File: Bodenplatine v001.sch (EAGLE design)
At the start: 3 parts, among them K8 RY210005

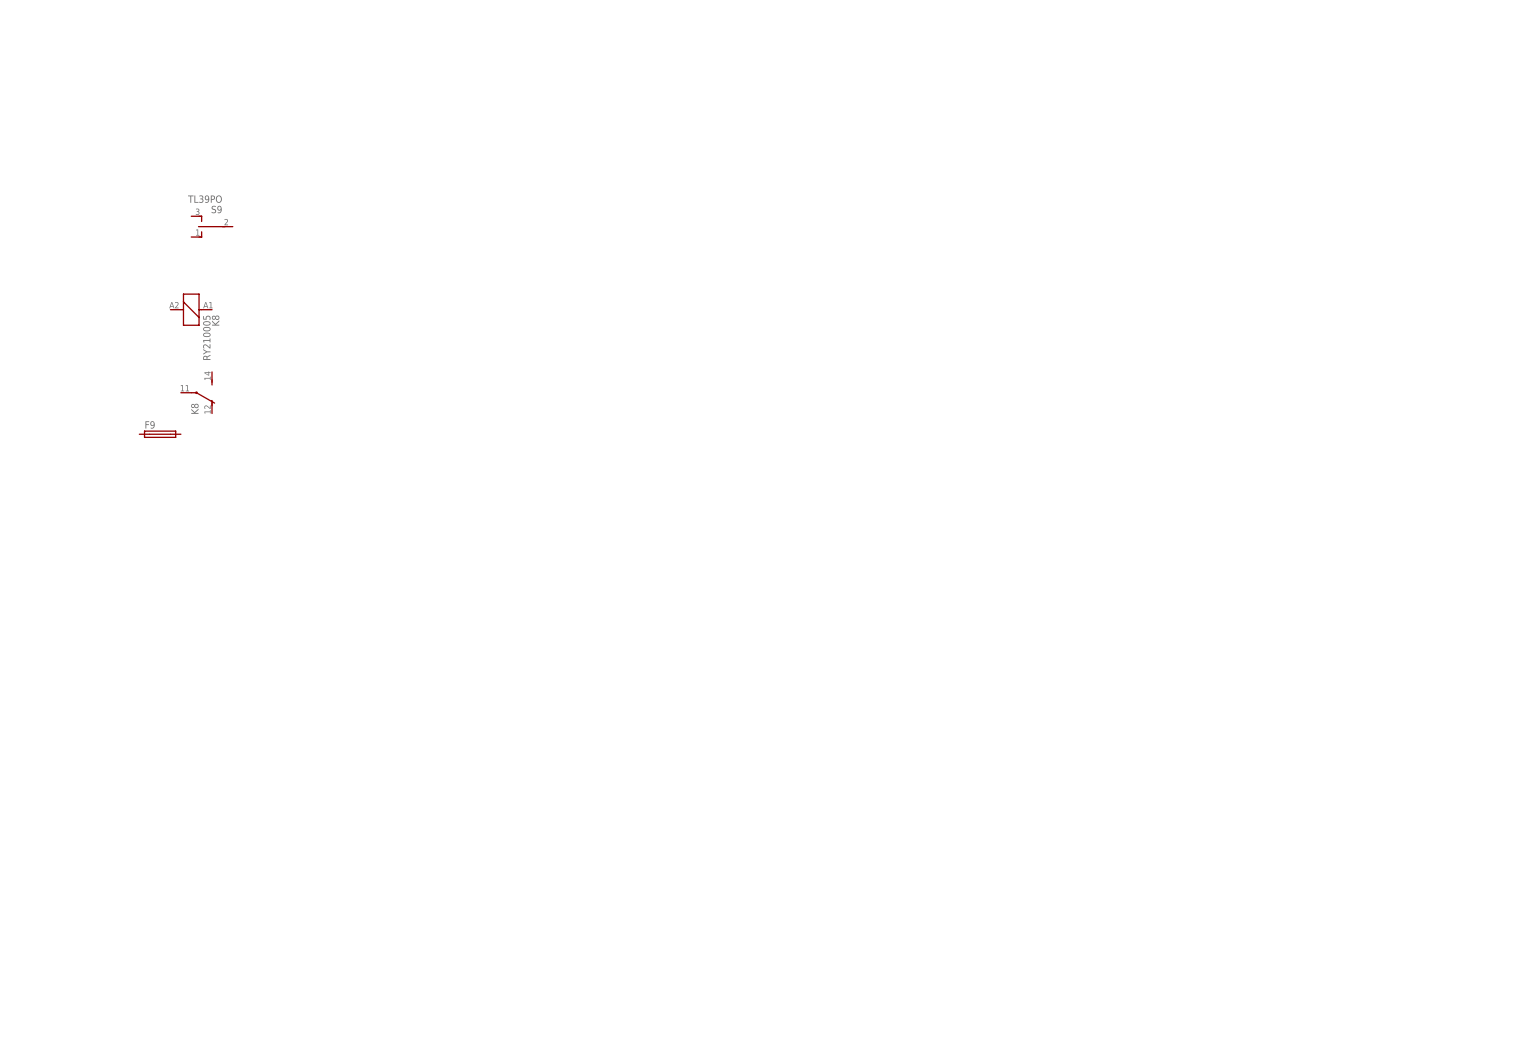
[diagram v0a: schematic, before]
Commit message: Erste fast fertige Version des Schaltplans der Bodebplatine
Es fehlt nur noch die Wago Klemme für L/N/PE Netzteil und 12V+/-
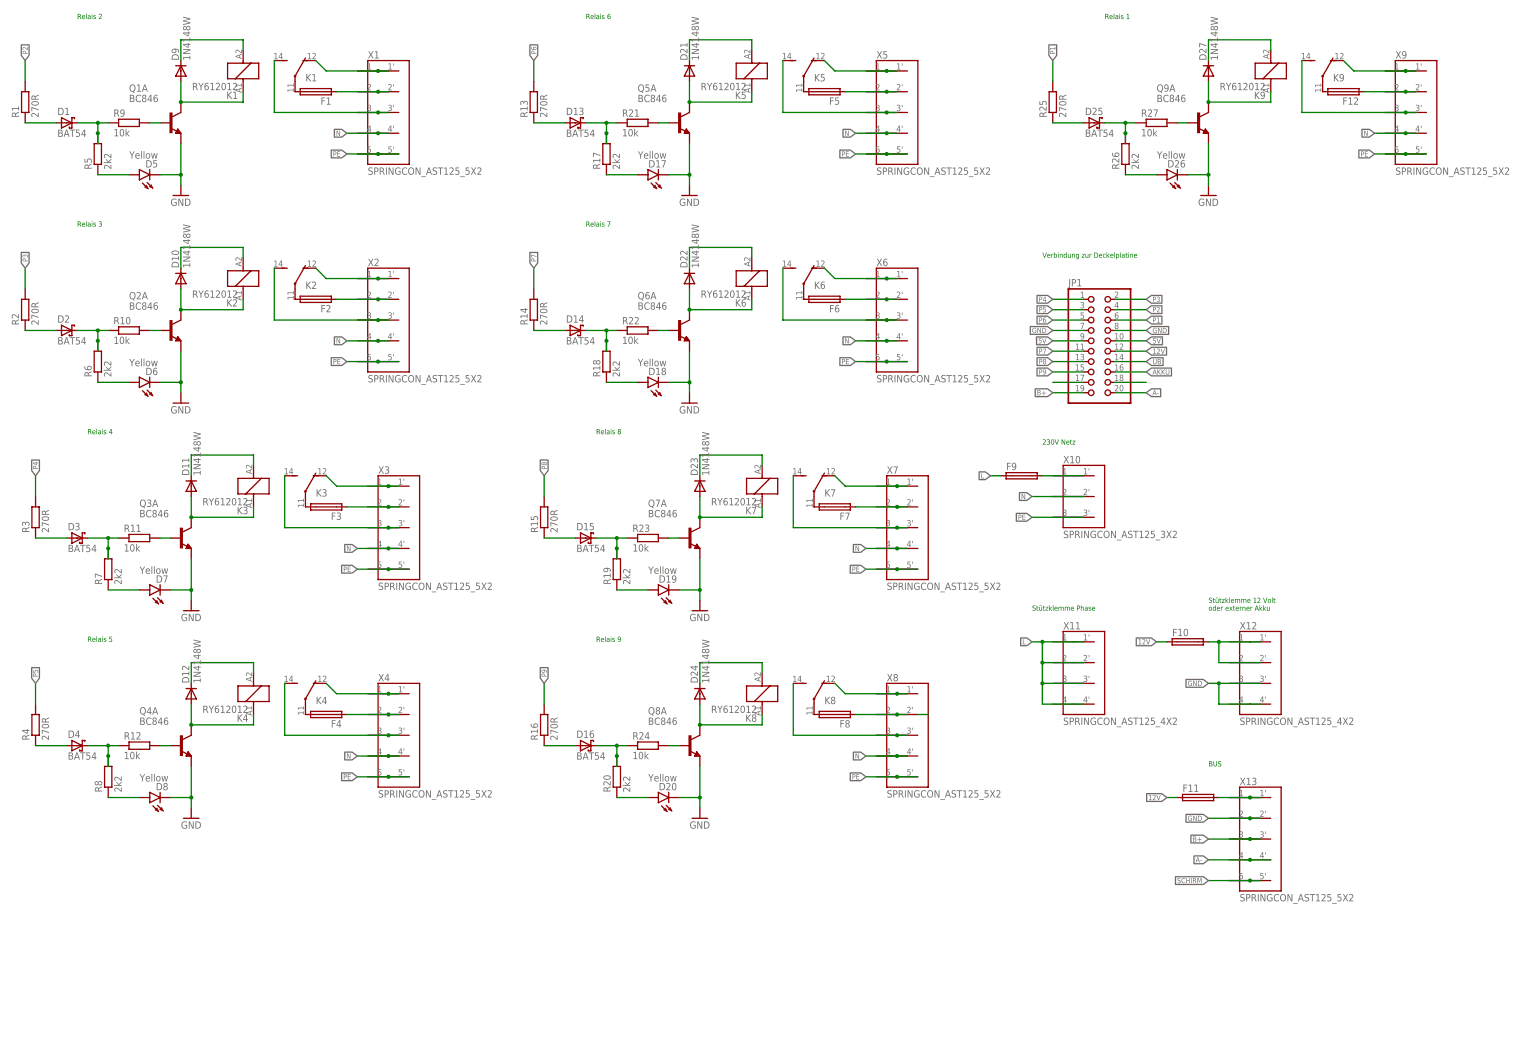
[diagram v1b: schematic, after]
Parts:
- removed S9: TL39PO, xMZ-Mod-Touch-Bodenplatine:TL39PO
- added D1, D13, D14, D15, D16, D2, D25, D3, D4: BAT54, diode:BAT54
- added D10, D11, D12, D21, D22, D23, D24, D27, D9: 1N4148W, diode:1N4148DO35-7
- added D17, D18, D19, D20, D26, D5, D6, D7, D8: Yellow, SparkFun-LED:LED-YELLOW0603
- added F1, F10, F11, F12, F2, F3, F4, F5, F6, F7, F8: (no value), xMZ-Mod-Touch-Bodenplatine:F456
- added JP1: (no value), pinhead:PINHD-2X10
- added K1, K2, K3, K4, K5, K6, K7, K9: RY612012, xMZ-Mod-Touch-Bodenplatine:RY612012
- added Q1, Q2, Q3, Q4, Q5, Q6, Q7, Q8, Q9: BC846, AWJLEagleLib:BC846BS"
- added R1, R13, R14, R15, R16, R2, R25, R3, R4: 270R, rcl:R-EU_M0805
- added R10, R11, R12, R21, R22, R23, R24, R27, R9: 10k, rcl:R-EU_R0603
- added R17, R18, R19, R20, R26, R5, R6, R7, R8: 2k2, rcl:R-EU_R0603
- added X1, X13, X2, X3, X4, X5, X6, X7, X8, X9: SPRINGCON_AST125_5X2, xMZ-Mod-Touch-Bodenplatine:SPRINGCON_AST125_5X2
- added X10: SPRINGCON_AST125_3X2, xMZ-Mod-Touch-Bodenplatine:SPRINGCON_AST125_3X2
- added X11, X12: SPRINGCON_AST125_4X2, xMZ-Mod-Touch-Bodenplatine:SPRINGCON_AST125_4X2
- K8: value RY210005 -> RY612012; device xMZ-Mod-Touch-Bodenplatine:RY210005 -> xMZ-Mod-Touch-Bodenplatine:RY612012
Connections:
- new net 12V: F10.1, F11.1, JP1.12
- new net 5V: JP1.10, JP1.9
- new net A-: JP1.20, X13.4@1, X13.4@2
- new net AKKU: JP1.16
- new net B+: JP1.19, X13.3@1
- new net GND: D17.C, D18.C, D19.C, D20.C, D26.C, D5.C, D6.C, D7.C, D8.C, JP1.7, JP1.8, Q1A.E, Q2A.E, Q3A.E, Q4A.E, Q5A.E, Q6A.E, Q7A.E, Q8A.E, Q9A.E, X13.2@1
- new net L: F9.1
- new net N: X1.4@1, X2.4@1, X3.4@1, X4.4@1, X5.4@1, X6.4@1, X7.4@1, X8.4@1, X9.4@1
- new net N$1: F1.1, X1.2@1
- new net N$10: Q1A.B, R9.2
- new net N$108: JP1.17
- new net N$11: D9.C, K11.2
- new net N$12: F2.2, K22.P
- new net N$13: D2.A, R2.1
- new net N$14: D2.C, R10.1, R6.2
- new net N$15: D6.A, R6.1
- new net N$16: Q2A.B, R10.2
- new net N$17: D10.C, K21.2
- new net N$18: D10.A, K21.1, Q2A.C
- new net N$19: F2.1, X2.2@1
- new net N$2: K12.S, X1.3@1
- new net N$20: K22.O, X2.1@1
- new net N$21: K32.S, X3.3@1
- new net N$22: F3.2, K32.P
- new net N$23: D3.A, R3.1
- new net N$24: D3.C, R11.1, R7.2
- new net N$25: D7.A, R7.1
- new net N$26: Q3A.B, R11.2
- new net N$27: D11.C, K31.2
- new net N$28: D11.A, K31.1, Q3A.C
- new net N$29: F3.1, X3.2@1
- new net N$3: F1.2, K12.P
- new net N$30: K32.O, X3.1@1
- new net N$31: K42.S, X4.3@1
- new net N$32: F4.2, K42.P
- new net N$33: D4.A, R4.1
- new net N$34: D4.C, R12.1, R8.2
- new net N$35: D8.A, R8.1
- new net N$36: Q4A.B, R12.2
- new net N$37: D12.C, K41.2
- new net N$38: D12.A, K41.1, Q4A.C
- new net N$39: F4.1, X4.2@1
- new net N$4: K12.O, X1.1@1
- new net N$40: K42.O, X4.1@1
- new net N$41: K52.S, X5.3@1
- new net N$42: F5.2, K52.P
- new net N$43: D13.A, R13.1
- new net N$44: D13.C, R17.2, R21.1
- new net N$45: D17.A, R17.1
- new net N$46: Q5A.B, R21.2
- new net N$47: D21.C, K51.2
- new net N$48: D21.A, K51.1, Q5A.C
- new net N$49: F5.1, X5.2@1
- new net N$5: D9.A, K11.1, Q1A.C
- new net N$50: K52.O, X5.1@1
- new net N$51: K62.S, X6.3@1
- new net N$52: F6.2, K62.P
- new net N$53: D14.A, R14.1
- new net N$54: D14.C, R18.2, R22.1
- new net N$55: D18.A, R18.1
- new net N$56: Q6A.B, R22.2
- new net N$57: D22.C, K61.2
- new net N$58: D22.A, K61.1, Q6A.C
- new net N$59: F6.1, X6.2@1
- new net N$6: K22.S, X2.3@1
- new net N$60: K62.O, X6.1@1
- new net N$61: K72.S, X7.3@1
- new net N$62: F7.2, K72.P
- new net N$63: D15.A, R15.1
- new net N$64: D15.C, R19.2, R23.1
- new net N$65: D19.A, R19.1
- new net N$66: Q7A.B, R23.2
- new net N$67: D23.C, K71.2
- new net N$68: D23.A, K71.1, Q7A.C
- new net N$69: F7.1, X7.2@1
- new net N$7: D1.A, R1.1
- new net N$70: K72.O, X7.1@1
- new net N$71: K82.S, X8.3@1
- new net N$72: F8.2, K82.P
- new net N$73: D16.A, R16.1
- new net N$74: D16.C, R20.2, R24.1
- new net N$75: D20.A, R20.1
- new net N$76: Q8A.B, R24.2
- new net N$77: D24.C, K81.2
- new net N$78: D24.A, K81.1, Q8A.C
- new net N$79: F8.1, X8.2@1
- new net N$8: D1.C, R5.2, R9.1
- new net N$80: K82.O, X8.1@1
- new net N$81: K92.S, X9.3@1
- new net N$82: F12.2, K92.P
- new net N$83: D25.A, R25.1
- new net N$84: D25.C, R26.2, R27.1
- new net N$85: D26.A, R26.1
- new net N$86: Q9A.B, R27.2
- new net N$87: D27.C, K91.2
- new net N$88: D27.A, K91.1, Q9A.C
- new net N$89: F12.1, X9.2@1
- new net N$9: D5.A, R5.1
- new net N$90: K92.O, X9.1@1
- new net N$91: F9.2
- new net N$92: F11.2, X13.1@1
- new net N$94: F10.2
- new net N$98: JP1.18
- new net P1: JP1.6, R25.2
- new net P2: JP1.4, R1.2
- new net P3: JP1.2, R2.2
- new net P4: JP1.1, R3.2
- new net P5: JP1.3, R4.2
- new net P6: JP1.5, R13.2
- new net P7: JP1.11, R14.2
- new net P8: JP1.13, R15.2
- new net P9: JP1.15, R16.2
- new net PE: X1.5@1, X1.5@2, X2.5@1, X2.5@2, X3.5@1, X3.5@2, X4.5@1, X4.5@2, X5.5@1, X5.5@2, X6.5@1, X6.5@2, X7.5@1, X7.5@2, X8.5@1, X8.5@2, X9.5@1, X9.5@2
- new net SCHIRM: X13.5@1
- new net UB: JP1.14
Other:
- note added: "230V Netz"
- note added: "BUS"
- note added: "Relais 1"
- note added: "Relais 2"
- note added: "Relais 3"
- note added: "Relais 4"
- note added: "Relais 5"
- note added: "Relais 6"
- note added: "Relais 7"
- note added: "Relais 8"
- note added: "Relais 9"
- note added: "Stützklemme 12 Volt oder externer Akku"
- note added: "Stützklemme Phase"
- note added: "Verbindung zur Deckelplatine"
- moved on the sheet: F9, K8

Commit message: Begin mit dem Bord der Bodenplatine
Schriften in den Schaltplänen einheitlich gemacht (Layer und Große)
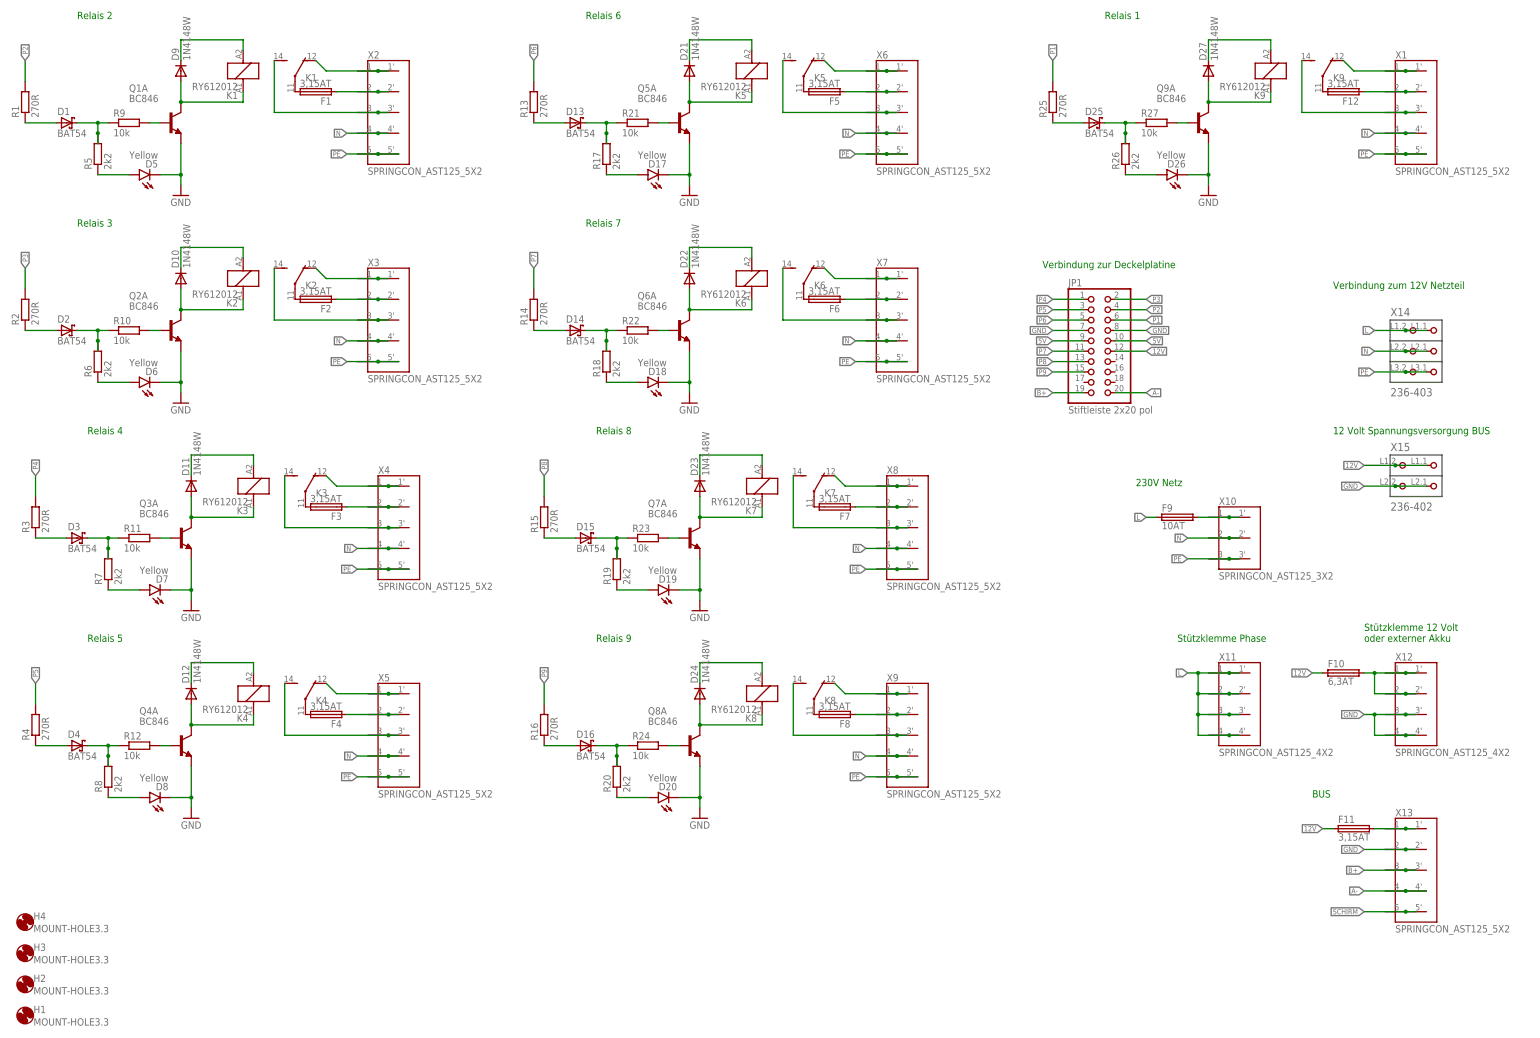
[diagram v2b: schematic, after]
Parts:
- added H1, H2, H3, H4: MOUNT-HOLE3.3, holes:MOUNT-HOLE3.3
- added X14: 236-403, con-wago_236:236-403
- added X15: 236-402, con-wago_236:236-402
- F1, F11, F12, F2, F3, F4, F5, F6, F7, F8: value (none) -> 3,15AT
- F10: value (none) -> 6,3AT
- F9: value (none) -> 10AT
- JP1: value (none) -> Stiftleiste 2x20 pol
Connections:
- removed net AKKU: JP1.16
- removed net N$108: JP1.17
- removed net N$98: JP1.18
- removed net UB: JP1.14
- net 12V: now also X15.P1.1, X15.P1.2
- net GND: now also X12.3@1, X12.4@1, X15.P2.1, X15.P2.2
- net L: now also X11.1@1, X11.2@1, X11.3@1, X11.4@1, X14.P1.1, X14.P1.2
- net N: now also X10.2@1, X14.P2.1, X14.P2.2
- net N$1: now also X2.2@1; no longer X1.2@1
- net N$19: now also X3.2@1; no longer X2.2@1
- net N$2: now also X2.3@1; no longer X1.3@1
- net N$20: now also X3.1@1; no longer X2.1@1
- net N$21: now also X4.3@1; no longer X3.3@1
- net N$29: now also X4.2@1; no longer X3.2@1
- net N$30: now also X4.1@1; no longer X3.1@1
- net N$31: now also X5.3@1; no longer X4.3@1
- net N$39: now also X5.2@1; no longer X4.2@1
- net N$4: now also X2.1@1; no longer X1.1@1
- net N$40: now also X5.1@1; no longer X4.1@1
- net N$41: now also X6.3@1; no longer X5.3@1
- net N$49: now also X6.2@1; no longer X5.2@1
- net N$50: now also X6.1@1; no longer X5.1@1
- net N$51: now also X7.3@1; no longer X6.3@1
- net N$59: now also X7.2@1; no longer X6.2@1
- net N$6: now also X3.3@1; no longer X2.3@1
- net N$60: now also X7.1@1; no longer X6.1@1
- net N$61: now also X8.3@1; no longer X7.3@1
- net N$69: now also X8.2@1; no longer X7.2@1
- net N$70: now also X8.1@1; no longer X7.1@1
- net N$71: now also X9.3@1; no longer X8.3@1
- net N$79: now also X9.2@1; no longer X8.2@1
- net N$80: now also X9.1@1; no longer X8.1@1
- net N$81: now also X1.3@1; no longer X9.3@1
- net N$89: now also X1.2@1; no longer X9.2@1
- net N$90: now also X1.1@1; no longer X9.1@1
- net N$91: now also X10.1@1
- net N$94: now also X12.1@1, X12.2@1
- net PE: now also X10.3@1, X14.P3.1, X14.P3.2
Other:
- note added: "12 Volt Spannungsversorgung BUS"
- note added: "Verbindung zum 12V Netzteil"
- moved on the sheet: F10, F11, F9, X1, X10, X11, X12, X13, X2, X3, X4, X5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
